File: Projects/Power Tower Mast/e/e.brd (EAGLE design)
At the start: 15.1 x 20.3 mm, 25 parts

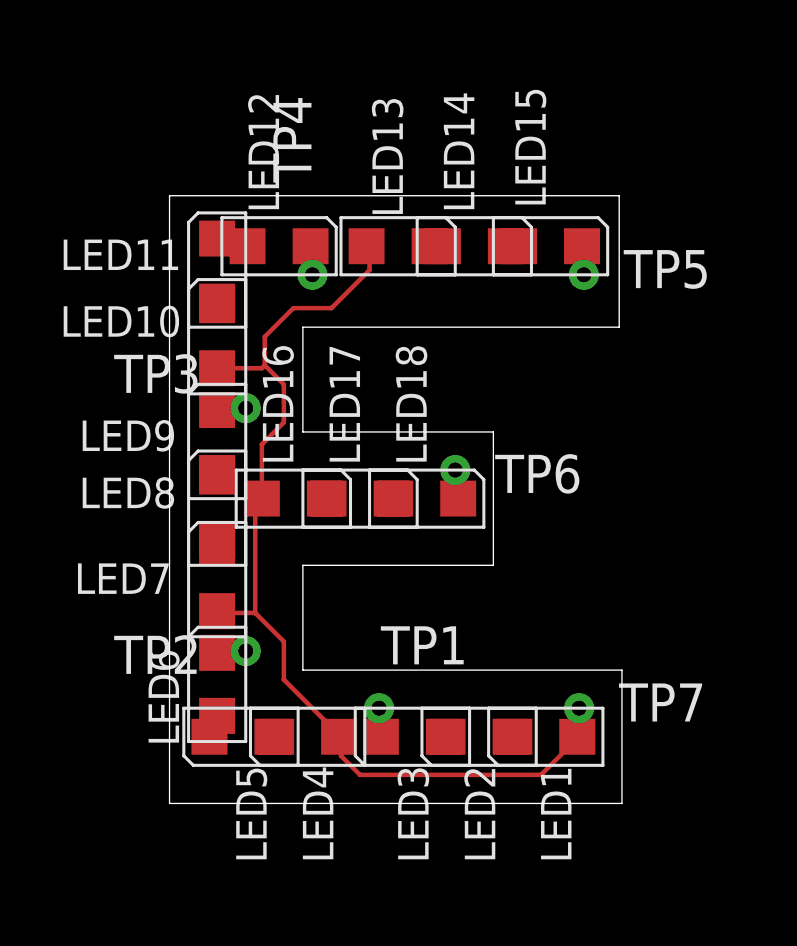
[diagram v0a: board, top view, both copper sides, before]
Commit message: updated with extra vias and panelized
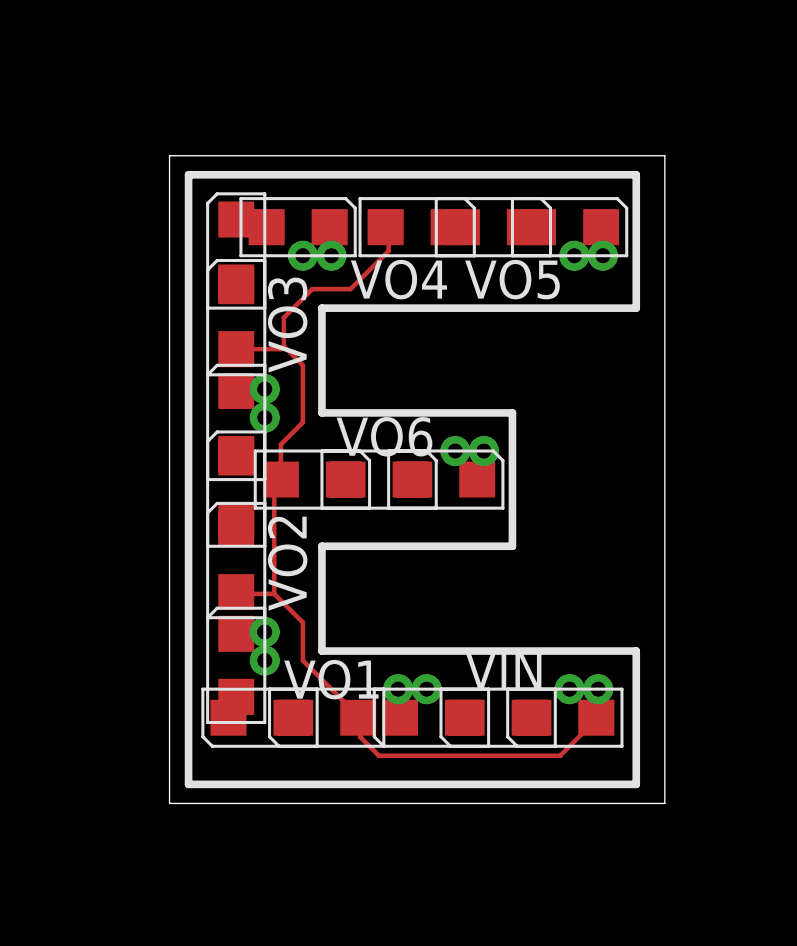
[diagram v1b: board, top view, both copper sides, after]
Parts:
- removed TP1, TP2, TP3, TP4, TP5, TP6, TP7: (no value), CyberRailGuru:P1-20
- added VIN, VIN1, VO1, VO10, VO11, VO12, VO2, VO3, VO4, VO5, VO6, VO7, VO8, VO9: (no value), CyberRailGuru:P1-20
- moved LED17 0.90 mm to (6.99, 10.8)
- moved LED10 0.90 mm to (2.22, 16.2)
- moved LED6 0.90 mm to (2.22, 4.60)
- moved LED7 0.90 mm to (2.22, 8.10)
- moved LED8 0.90 mm to (2.22, 10.5)
- moved LED9 0.90 mm to (2.22, 12.7)
- moved LED1 0.90 mm to (13.2, 2.86)
- moved LED15 0.90 mm to (13.3, 19.2)
- moved LED16 0.90 mm to (4.76, 10.8)
- moved LED18 0.90 mm to (9.21, 10.8)
- moved LED2 0.90 mm to (11.0, 2.86)
- moved LED3 0.90 mm to (8.73, 2.86)
- moved LED4 0.90 mm to (5.24, 2.86)
- moved LED5 0.90 mm to (3.02, 2.86)
- moved LED13 0.90 mm to (8.26, 19.2)
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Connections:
- removed net VIN4: LED1.A, LED10.A, LED13.A, LED16.A, LED4.A, LED7.A, TP7.TP
- removed net VOUT20: LED3.C, TP1.TP
- removed net VOUT21: LED6.C, TP2.TP
- removed net VOUT22: LED9.C, TP3.TP
- removed net VOUT23: LED12.C, TP4.TP
- removed net VOUT24: LED15.C, TP5.TP
- removed net VOUT25: LED18.C, TP6.TP
- new net VIN: LED1.A, LED10.A, LED13.A, LED16.A, LED4.A, LED7.A, VIN.TP, VIN1.TP
- new net VOUT1: LED3.C, VO1.TP, VO7.TP
- new net VOUT2: LED6.C, VO2.TP, VO8.TP
- new net VOUT3: LED9.C, VO3.TP, VO9.TP
- new net VOUT4: LED12.C, VO10.TP, VO4.TP
- new net VOUT5: LED15.C, VO11.TP, VO5.TP
- new net VOUT6: LED18.C, VO12.TP, VO6.TP
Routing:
- net VIN: track 0.00 -> 34.6 mm
- net VIN4: track 33.7 -> 0.00 mm
- net VOUT6: track 0.00 -> 2.00 mm
- net VOUT1: track 0.00 -> 1.93 mm
- net VOUT2: track 0.00 -> 1.93 mm
- net VOUT3: track 0.00 -> 1.93 mm
- net VOUT5: track 0.00 -> 1.93 mm
- net VOUT4: track 0.00 -> 1.89 mm
- net VOUT25: track 0.99 -> 0.00 mm
- net VOUT23: track 0.98 -> 0.00 mm
- net VOUT21: track 0.98 -> 0.00 mm
- net VOUT24: track 0.98 -> 0.00 mm
- net VOUT22: track 0.98 -> 0.00 mm
- net VOUT20: track 0.98 -> 0.00 mm
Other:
- board size 15.1 x 20.3 mm -> 16.5 x 21.6 mm

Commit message: reworking some letters
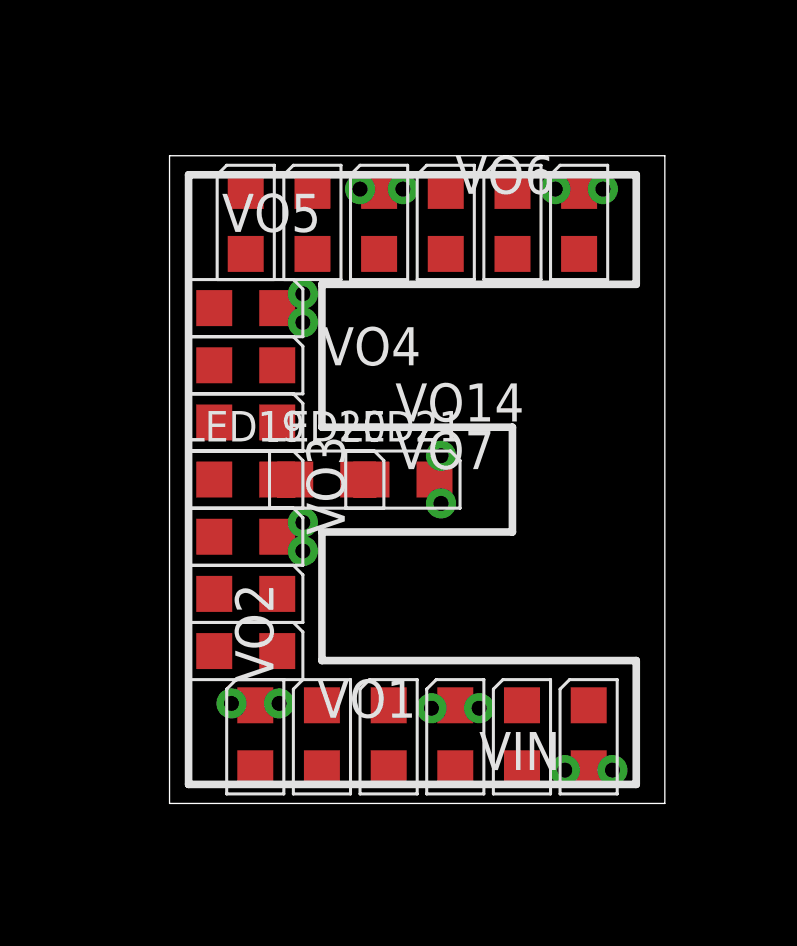
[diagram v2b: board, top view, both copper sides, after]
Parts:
- added LED19, LED20, LED21: (no value), CyberRailGuru:LED_0805
- added VO13, VO14: (no value), CyberRailGuru:P1-20
- moved LED16 9.66 mm to (9.21, 19.4), turned to 0 degrees
- moved LED17 9.66 mm to (11.4, 19.4), turned to 0 degrees
- moved LED18 9.66 mm to (13.7, 19.4), turned to 0 degrees
- moved VO6 9.59 mm to (14.4, 20.5)
- moved VO9 9.54 mm to (3.65, 3.33)
- moved VO11 9.14 mm to (4.45, 17.0)
- moved VO12 8.90 mm to (7.78, 20.5)
- moved VO10 8.89 mm to (4.45, 9.37)
- moved VO5 8.40 mm to (6.35, 20.5)
- moved VO8 7.32 mm to (10.3, 3.17)
- moved LED15 6.35 mm to (6.99, 19.4), turned to 0 degrees
- moved VO7 6.21 mm to (9.05, 10.0)
- moved LED14 6.03 mm to (4.76, 19.4), turned to 0 degrees
- moved LED13 5.72 mm to (2.54, 19.4), turned to 0 degrees
- moved VO3 5.54 mm to (4.45, 8.41)
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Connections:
- new net N$1: LED19.C, LED20.A
- new net N$2: LED20.C, LED21.A
- new net N$3: LED21.C, VO14.TP, VO7.TP
- net VIN: now also LED19.A
- net VOUT1: now also VO8.TP; no longer VO7.TP
- net VOUT2: now also VO9.TP; no longer VO8.TP
- net VOUT3: now also VO10.TP; no longer VO9.TP
- net VOUT4: now also VO11.TP; no longer VO10.TP
- net VOUT5: now also VO12.TP; no longer VO11.TP
- net VOUT6: now also VO13.TP; no longer VO12.TP
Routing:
- net VIN: track 34.6 -> 0.00 mm
- net VOUT6: track 2.00 -> 0.00 mm
- net VOUT1: track 1.93 -> 0.00 mm
- net VOUT2: track 1.93 -> 0.00 mm
- net VOUT3: track 1.93 -> 0.00 mm
- net VOUT5: track 1.93 -> 0.00 mm
- net VOUT4: track 1.89 -> 0.00 mm
- net N$45: track 1.12 -> 0.00 mm
- net N$41: track 0.80 -> 0.00 mm

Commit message: final updates before fab.  added new letters for future projects.
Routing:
- net VIN: track 0.00 -> 41.5 mm, vias 0 -> 5
- net N$50: track 0.00 -> 3.09 mm
- net N$49: track 0.00 -> 3.09 mm
- net N$48: track 0.00 -> 3.09 mm
- net N$47: track 0.00 -> 3.09 mm
- net N$39: track 0.00 -> 3.09 mm
- net N$41: track 0.00 -> 3.09 mm
- net N$42: track 0.00 -> 3.09 mm
- net N$40: track 0.00 -> 3.09 mm
- net N$46: track 0.00 -> 2.89 mm
- net N$45: track 0.00 -> 2.89 mm
- net N$44: track 0.00 -> 2.89 mm
- net N$43: track 0.00 -> 2.89 mm
- net N$3: track 0.00 -> 2.47 mm
- net VOUT3: track 0.00 -> 2.00 mm
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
